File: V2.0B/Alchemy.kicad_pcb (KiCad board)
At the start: 4 copper layers, 55 x 85 mm, 65 parts, among them J1 Conn_02x20_Odd_Even, J2 USB_C_Receptacle_USB2.0, J3 USB_C_Receptacle_USB2.0, J4 Conn_01x03, J5 Conn_01x03, J6 Conn_01x02, J7 Conn_01x02, J8 Conn_01x02, J9 Conn_01x03, U1 CH32V203C8T6, U2 HT1015A, U3 CH213K, U4 AMS1117-3.3, U5 CH213K, U6 MT9700, Y2 8MHz

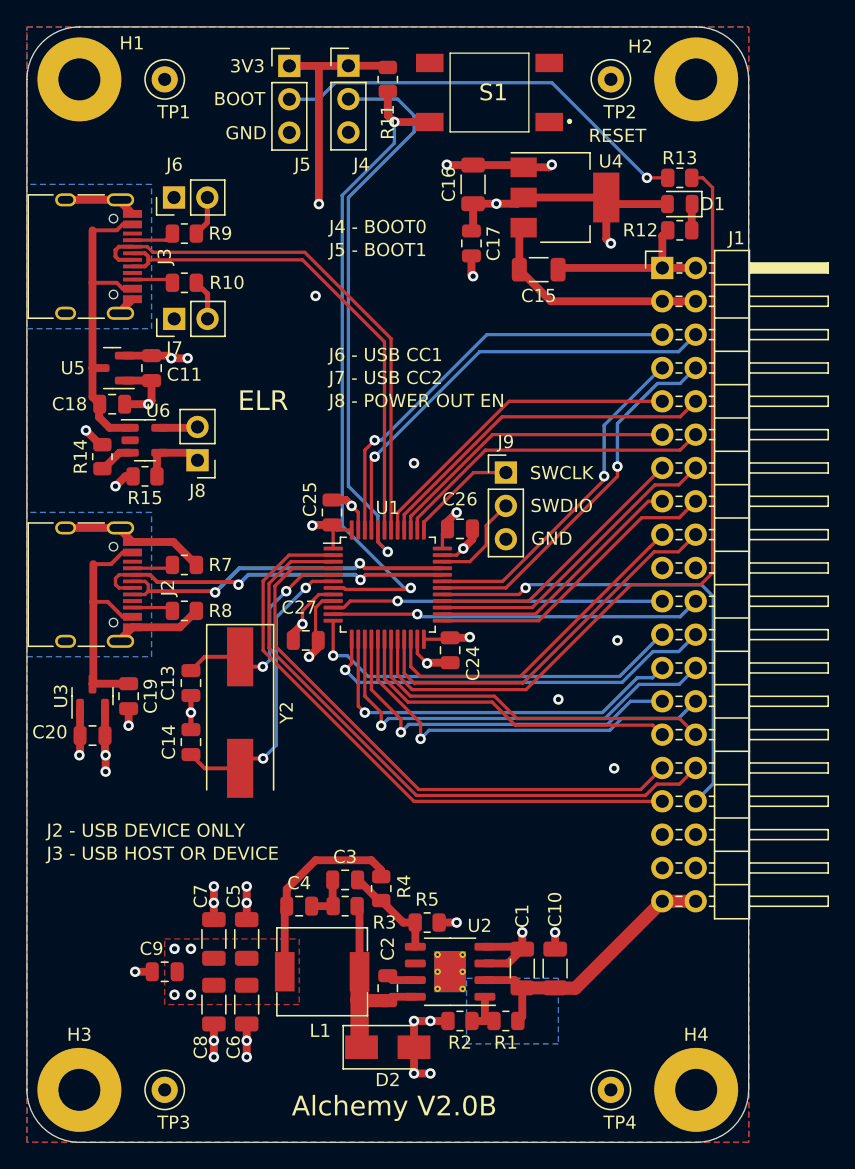
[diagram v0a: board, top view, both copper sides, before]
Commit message: Minor layout fixes
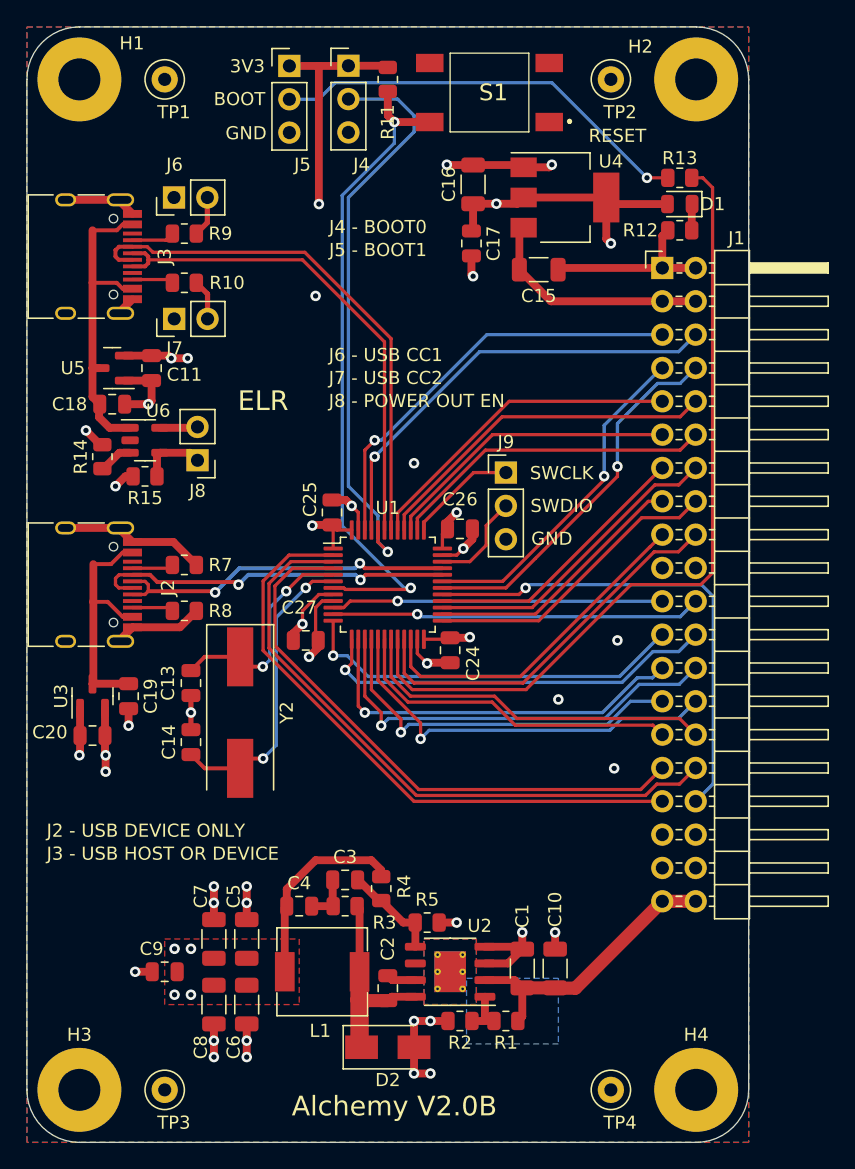
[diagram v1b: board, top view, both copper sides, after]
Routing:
- added copper zone on In2.Cu, net GND
